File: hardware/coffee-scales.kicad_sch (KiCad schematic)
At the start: 6 parts, among them J1 Conn_01x04, SW1 SW_Push, U1 Adafruit_Feather_328P, U2 HX711_Breakout, U3 4DIGIT_7SEG, U4 4DIGIT_7SEG

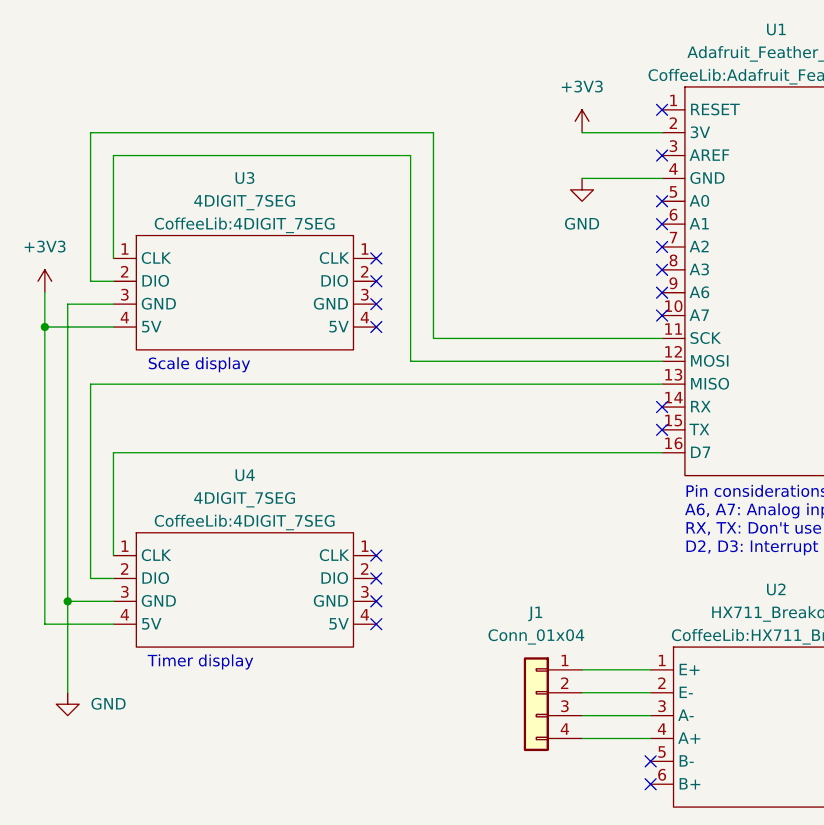
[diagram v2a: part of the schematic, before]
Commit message: Big but pointless PCB update
* Rounded corners
* Components not so close to the edge
* HX711 data pin on interrupt
* Bigger vias/pads
* Square first pad
* Lots of stuff added to silkscreen

But my gut feeling is the next PCB I have made will be without
all the breakouts anyway.
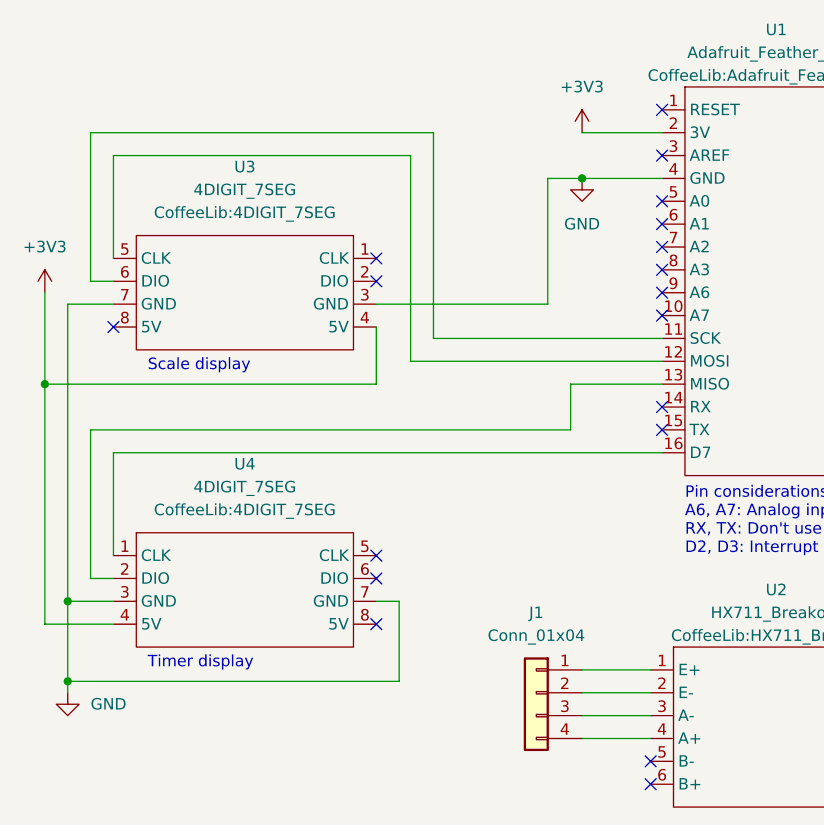
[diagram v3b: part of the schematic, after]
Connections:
- net GND: now also U3.7 (GND), U4.7 (GND)
- net at U1.11 (SCK): now also U3.6 (DIO); no longer U3.2 (DIO)
- net at U1.12 (MOSI): now also U3.5 (CLK); no longer U3.1 (CLK)
- no-connect marks 29 -> 27
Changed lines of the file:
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@@
   (junction (at 53.34 138.43) (diameter 0) (color 0 0 0 0)
   )
-  (junction (at 50.8 107.95) (diameter 0) (color 0 0 0 0)
+  (junction (at 53.34 147.32) (diameter 0) (color 0 0 0 0)
+  )
+  (junction (at 50.8 114.3) (diameter 0) (color 0 0 0 0)
+  )
+  (junction (at 110.49 91.44) (diameter 0) (color 0 0 0 0)
   )
   (no_connect (at 144.78 114.3))
@@
   (no_connect (at 144.78 109.22))
   (no_connect (at 144.78 116.84))
+  (no_connect (at 58.42 107.95))
   (no_connect (at 87.63 135.89))
   (no_connect (at 87.63 140.97))
-  (no_connect (at 87.63 138.43))
   (no_connect (at 87.63 133.35))
-  (no_connect (at 87.63 105.41))
-  (no_connect (at 87.63 107.95))
   (no_connect (at 87.63 102.87))
   (no_connect (at 87.63 100.33))
@@
     (stroke (width 0) (type default) (color 0 0 0 0))
   )
+  (wire (pts (xy 90.17 138.43) (xy 90.17 147.32))
+    (stroke (width 0) (type default) (color 0 0 0 0))
+  )
   (wire (pts (xy 58.42 88.9) (xy 91.44 88.9))
     (stroke (width 0) (type default) (color 0 0 0 0))
   )
-  (wire (pts (xy 55.88 114.3) (xy 119.38 114.3))
-    (stroke (width 0) (type default) (color 0 0 0 0))
-  )
   (wire (pts (xy 144.78 104.14) (xy 151.13 104.14))
     (stroke (width 0) (type default) (color 0 0 0 0))
   )
-  (wire (pts (xy 50.8 107.95) (xy 58.42 107.95))
+  (wire (pts (xy 55.88 119.38) (xy 109.22 119.38))
+    (stroke (width 0) (type default) (color 0 0 0 0))
+  )
+  (wire (pts (xy 119.38 114.3) (xy 109.22 114.3))
     (stroke (width 0) (type default) (color 0 0 0 0))
   )
@@
     (stroke (width 0) (type default) (color 0 0 0 0))
   )
-  (wire (pts (xy 53.34 138.43) (xy 53.34 148.59))
+  (wire (pts (xy 53.34 138.43) (xy 53.34 147.32))
     (stroke (width 0) (type default) (color 0 0 0 0))
   )
@@
     (stroke (width 0) (type default) (color 0 0 0 0))
   )
-  (wire (pts (xy 55.88 114.3) (xy 55.88 135.89))
+  (wire (pts (xy 87.63 105.41) (xy 106.68 105.41))
     (stroke (width 0) (type default) (color 0 0 0 0))
   )
@@
     (stroke (width 0) (type default) (color 0 0 0 0))
   )
+  (wire (pts (xy 55.88 119.38) (xy 55.88 135.89))
+    (stroke (width 0) (type default) (color 0 0 0 0))
+  )
   (wire (pts (xy 110.49 91.44) (xy 119.38 91.44))
     (stroke (width 0) (type default) (color 0 0 0 0))
@@
     (stroke (width 0) (type default) (color 0 0 0 0))
   )
+  (wire (pts (xy 50.8 114.3) (xy 87.63 114.3))
+    (stroke (width 0) (type default) (color 0 0 0 0))
+  )
+  (wire (pts (xy 106.68 105.41) (xy 106.68 91.44))
+    (stroke (width 0) (type default) (color 0 0 0 0))
+  )
   (wire (pts (xy 55.88 102.87) (xy 58.42 102.87))
     (stroke (width 0) (type default) (color 0 0 0 0))
@@
     (stroke (width 0) (type default) (color 0 0 0 0))
   )
-  (wire (pts (xy 50.8 140.97) (xy 50.8 107.95))
+  (wire (pts (xy 50.8 104.14) (xy 50.8 114.3))
+    (stroke (width 0) (type default) (color 0 0 0 0))
+  )
+  (wire (pts (xy 106.68 91.44) (xy 110.49 91.44))
     (stroke (width 0) (type default) (color 0 0 0 0))
   )
@@
     (stroke (width 0) (type default) (color 0 0 0 0))
   )
+  (wire (pts (xy 53.34 147.32) (xy 90.17 147.32))
+    (stroke (width 0) (type default) (color 0 0 0 0))
+  )
   (wire (pts (xy 58.42 88.9) (xy 58.42 100.33))
     (stroke (width 0) (type default) (color 0 0 0 0))
@@
     (stroke (width 0) (type default) (color 0 0 0 0))
   )
-  (wire (pts (xy 50.8 104.14) (xy 50.8 107.95))
+  (wire (pts (xy 53.34 147.32) (xy 53.34 148.59))
     (stroke (width 0) (type default) (color 0 0 0 0))
   )
@@
     (stroke (width 0) (type default) (color 0 0 0 0))
   )
+  (wire (pts (xy 87.63 107.95) (xy 87.63 114.3))
+    (stroke (width 0) (type default) (color 0 0 0 0))
+  )
+  (wire (pts (xy 109.22 114.3) (xy 109.22 119.38))
+    (stroke (width 0) (type default) (color 0 0 0 0))
+  )
   (wire (pts (xy 158.75 153.67) (xy 158.75 121.92))
     (stroke (width 0) (type default) (color 0 0 0 0))
   )
   (wire (pts (xy 146.05 156.21) (xy 148.59 156.21))
+    (stroke (width 0) (type default) (color 0 0 0 0))
+  )
+  (wire (pts (xy 87.63 138.43) (xy 90.17 138.43))
+    (stroke (width 0) (type default) (color 0 0 0 0))
+  )
+  (wire (pts (xy 50.8 114.3) (xy 50.8 140.97))
     (stroke (width 0) (type default) (color 0 0 0 0))
   )
@@
     (pin "1")
   )
-  (symbol (lib_id "CoffeeLib:4DIGIT_7SEG") (at 73.66 137.16 0) (unit 1)
-    (in_bom yes) (on_board yes) (fields_autoplaced)
-    (property "Reference" "U4" (id 0) (at 73.025 124.46 0))
-    (property "Value" "4DIGIT_7SEG" (id 1) (at 73.025 127 0))
-    (property "Footprint" "CoffeeLib:4DIGIT_7SEG" (id 2) (at 73.025 129.54 0))
+  (symbol (lib_name "4DIGIT_7SEG_1") (lib_id "CoffeeLib:4DIGIT_7SEG") (at 73.66 137.16 0) (unit 1)
+    (in_bom yes) (on_board yes) (fields_autoplaced)
+    (property "Reference" "U4" (id 0) (at 73.025 123.19 0))
+    (property "Value" "4DIGIT_7SEG" (id 1) (at 73.025 125.73 0))
+    (property "Footprint" "CoffeeLib:4DIGIT_7SEG" (id 2) (at 73.025 128.27 0))
     (property "Datasheet" "" (id 3) (at 73.66 137.16 0)
       (effects (font (size 1.27 1.27)) hide)
     )
     (pin "1")
-    (pin "1")
-    (pin "2")
     (pin "2")
     (pin "3")
+    (pin "4")
+    (pin "5")
+    (pin "6")
+    (pin "7")
+    (pin "8")
+  )
+  (symbol (lib_id "power:+3V3") (at 110.49 86.36 0) (unit 1)
+    (in_bom yes) (on_board yes) (fields_autoplaced)
+    (property "Reference" "#PWR0101" (id 0) (at 110.49 90.17 0)
+      (effects (font (size 1.27 1.27)) hide)
+    )
+    (property "Value" "+3V3" (id 1) (at 110.49 81.28 0))
+    (property "Footprint" "" (id 2) (at 110.49 86.36 0)
+      (effects (font (size 1.27 1.27)) hide)
+    )
+    (property "Datasheet" "" (id 3) (at 110.49 86.36 0)
+      (effects (font (size 1.27 1.27)) hide)
+    )
+    (pin "1")
+  )
+  (symbol (lib_id "power:+3V3") (at 50.8 104.14 0) (unit 1)
+    (in_bom yes) (on_board yes) (fields_autoplaced)
+    (property "Reference" "#PWR01" (id 0) (at 50.8 107.95 0)
+      (effects (font (size 1.27 1.27)) hide)
+    )
+    (property "Value" "+3V3" (id 1) (at 50.8 99.06 0))
+    (property "Footprint" "" (id 2) (at 50.8 104.14 0)
+      (effects (font (size 1.27 1.27)) hide)
+    )
+    (property "Datasheet" "" (id 3) (at 50.8 104.14 0)
+      (effects (font (size 1.27 1.27)) hide)
+    )
+    (pin "1")
+  )
+  (symbol (lib_id "power:GND") (at 53.34 148.59 0) (unit 1)
+    (in_bom yes) (on_board yes) (fields_autoplaced)
+    (property "Reference" "#PWR02" (id 0) (at 53.34 154.94 0)
+      (effects (font (size 1.27 1.27)) hide)
+    )
+    (property "Value" "GND" (id 1) (at 55.88 149.8599 0)
+      (effects (font (size 1.27 1.27)) (justify left))
+    )
+    (property "Footprint" "" (id 2) (at 53.34 148.59 0)
+      (effects (font (size 1.27 1.27)) hide)
+    )
+    (property "Datasheet" "" (id 3) (at 53.34 148.59 0)
+      (effects (font (size 1.27 1.27)) hide)
+    )
+    (pin "1")
+  )
+  (symbol (lib_id "CoffeeLib:4DIGIT_7SEG") (at 72.39 104.14 0) (mirror y) (unit 1)
+    (in_bom yes) (on_board yes) (fields_autoplaced)
+    (property "Reference" "U3" (id 0) (at 73.025 90.17 0))
+    (property "Value" "4DIGIT_7SEG" (id 1) (at 73.025 92.71 0))
+    (property "Footprint" "CoffeeLib:4DIGIT_7SEG" (id 2) (at 73.025 95.25 0))
+    (property "Datasheet" "" (id 3) (at 72.39 104.14 0)
+      (effects (font (size 1.27 1.27)) hide)
+    )
+    (pin "1")
+    (pin "2")
     (pin "3")
     (pin "4")
-    (pin "4")
-  )
-  (symbol (lib_id "power:+3V3") (at 110.49 86.36 0) (unit 1)
-    (in_bom yes) (on_board yes) (fields_autoplaced)
-    (property "Reference" "#PWR0101" (id 0) (at 110.49 90.17 0)
-      (effects (font (size 1.27 1.27)) hide)
-    )
-    (property "Value" "+3V3" (id 1) (at 110.49 81.28 0))
-    (property "Footprint" "" (id 2) (at 110.49 86.36 0)
-      (effects (font (size 1.27 1.27)) hide)
-    )
-    (property "Datasheet" "" (id 3) (at 110.49 86.36 0)
-      (effects (font (size 1.27 1.27)) hide)
-    )
-    (pin "1")
-  )
-  (symbol (lib_id "power:+3V3") (at 50.8 104.14 0) (unit 1)
-    (in_bom yes) (on_board yes) (fields_autoplaced)
-    (property "Reference" "#PWR01" (id 0) (at 50.8 107.95 0)
-      (effects (font (size 1.27 1.27)) hide)
-    )
-    (property "Value" "+3V3" (id 1) (at 50.8 99.06 0))
-    (property "Footprint" "" (id 2) (at 50.8 104.14 0)
-      (effects (font (size 1.27 1.27)) hide)
-    )
-    (property "Datasheet" "" (id 3) (at 50.8 104.14 0)
-      (effects (font (size 1.27 1.27)) hide)
-    )
-    (pin "1")
-  )
-  (symbol (lib_id "power:GND") (at 53.34 148.59 0) (unit 1)
-    (in_bom yes) (on_board yes) (fields_autoplaced)
-    (property "Reference" "#PWR02" (id 0) (at 53.34 154.94 0)
-      (effects (font (size 1.27 1.27)) hide)
-    )
-    (property "Value" "GND" (id 1) (at 55.88 149.8599 0)
-      (effects (font (size 1.27 1.27)) (justify left))
-    )
-    (property "Footprint" "" (id 2) (at 53.34 148.59 0)
-      (effects (font (size 1.27 1.27)) hide)
-    )
-    (property "Datasheet" "" (id 3) (at 53.34 148.59 0)
-      (effects (font (size 1.27 1.27)) hide)
-    )
-    (pin "1")
-  )
-  (symbol (lib_id "CoffeeLib:4DIGIT_7SEG") (at 73.66 104.14 0) (unit 1)
-    (in_bom yes) (on_board yes) (fields_autoplaced)
-    (property "Reference" "U3" (id 0) (at 73.025 91.44 0))
-    (property "Value" "4DIGIT_7SEG" (id 1) (at 73.025 93.98 0))
-    (property "Footprint" "CoffeeLib:4DIGIT_7SEG" (id 2) (at 73.025 96.52 0))
-    (property "Datasheet" "" (id 3) (at 73.66 104.14 0)
-      (effects (font (size 1.27 1.27)) hide)
-    )
-    (pin "1")
-    (pin "1")
-    (pin "2")
-    (pin "2")
-    (pin "3")
-    (pin "3")
-    (pin "4")
-    (pin "4")
+    (pin "5")
+    (pin "6")
+    (pin "7")
+    (pin "8")
   )
   (symbol (lib_id "power:GND") (at 110.49 91.44 0) (unit 1)

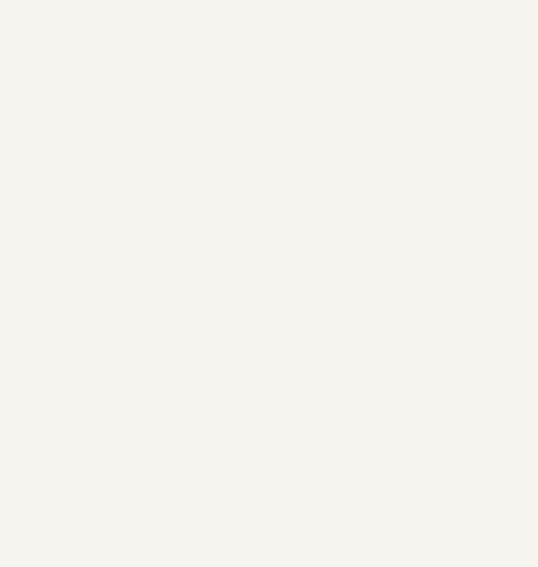
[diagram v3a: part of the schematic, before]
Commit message: Add (unmodified) Sparkfun HX711 breakout schematic
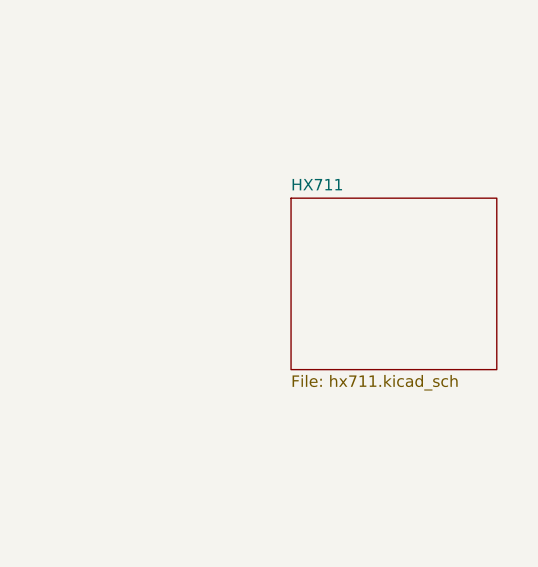
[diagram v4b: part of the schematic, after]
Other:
- added sheet HX711 (hx711.kicad_sch)

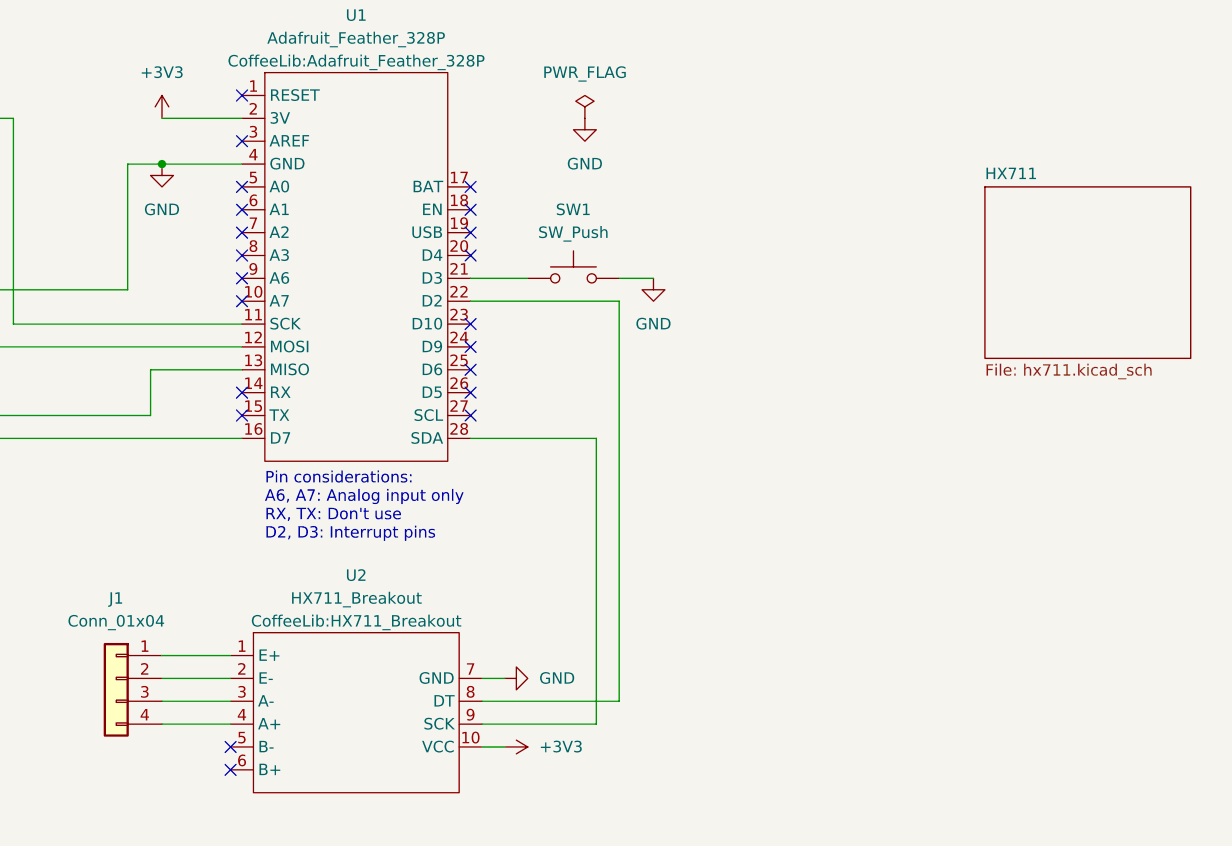
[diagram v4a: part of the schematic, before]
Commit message: Integrate HX711 sub-schematic
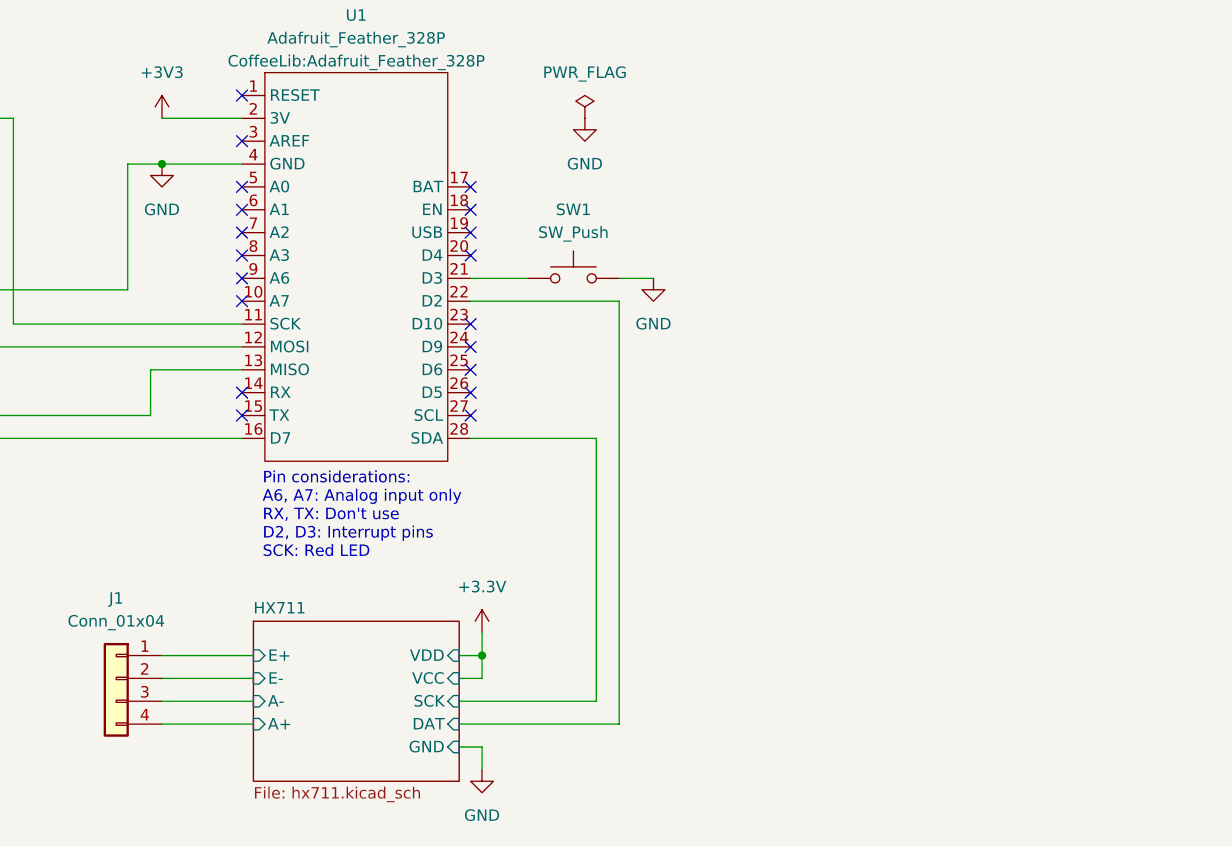
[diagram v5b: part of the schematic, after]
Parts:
- removed U2: HX711_Breakout, CoffeeLib:HX711_Breakout, symbol CoffeeLib:HX711_Breakout
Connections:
- net HX711/DAT: now reaches U1.22 (D2)
- net HX711/SCK: now reaches U1.28 (SDA)
- net HX711/E+: now reaches J1.1 (Pin_1)
- net HX711/E-: now reaches J1.2 (Pin_2)
- net HX711/A-: now reaches J1.3 (Pin_3)
- net HX711/A+: now reaches J1.4 (Pin_4)
- no-connect marks 27 -> 25
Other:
- sheet HX711 ports: added A+, A-, DAT, E+, E-, GND, SCK, VCC, VDD; removed none
- note added: "Pin considerations: A6, A7: Analog input only RX, TX: Don't use D2, D3: Interrupt pins SCK: Red LED"
- note removed: "Pin considerations: A6, A7: Analog input only RX, TX: Don't use D2, D3: Interrupt pins"

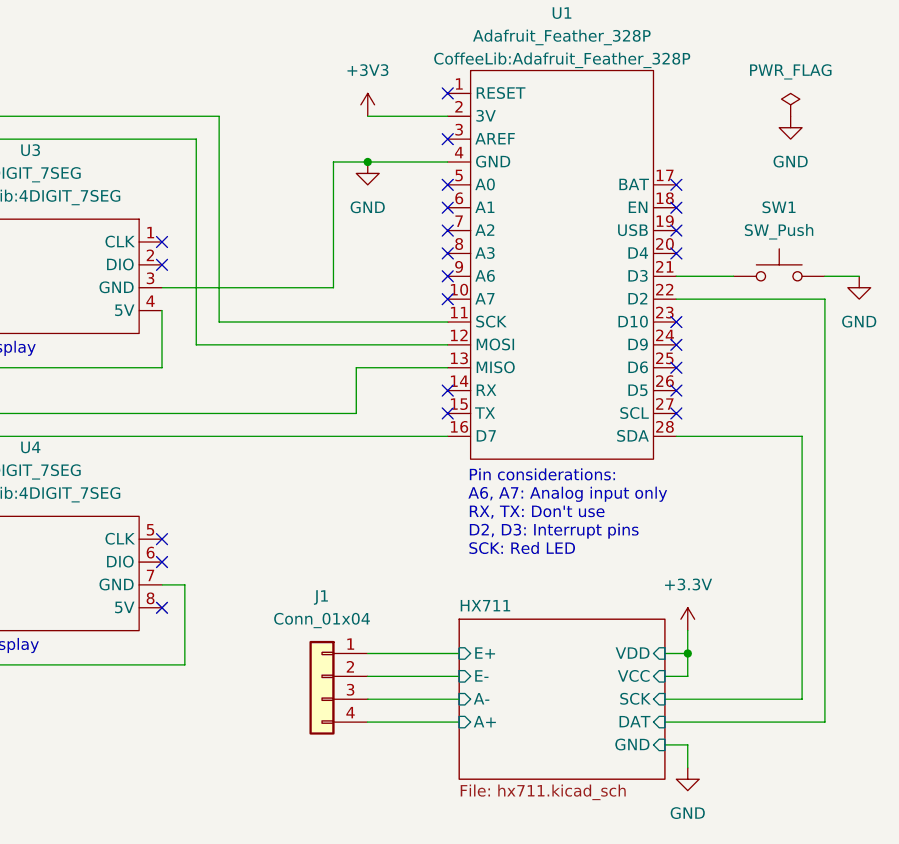
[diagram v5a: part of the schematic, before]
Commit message: Finish HX711 integration
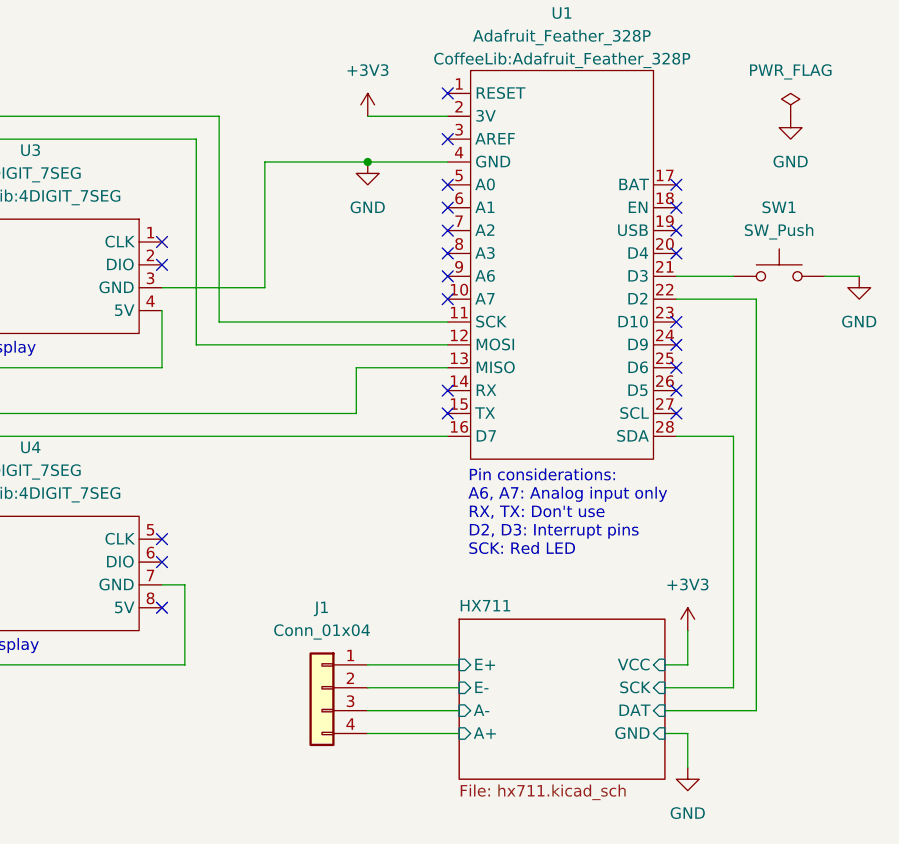
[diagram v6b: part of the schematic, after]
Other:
- sheet HX711 ports: added none; removed VDD
- moved on the sheet: J1
